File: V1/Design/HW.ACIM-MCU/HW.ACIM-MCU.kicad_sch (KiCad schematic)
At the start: 48 parts, among them J1 HEADER 2x15POS, J2 HEADER 2x15POS, U1 MIPS 32-bit DSC, U2 12MHz

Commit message: MCU PIM schematic update 5
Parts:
- removed C1, C11, C14, C15, C16, C17, C18, C2, C3, C4, C5, C6, C7, C8, C9: 22pF, SAMPI:CAP0402, symbol SAMPI:CERCAP
- removed R10, R11, R12, R13, R14, R2, R3, R4, R5, R6, R7, R8, R9: 10R, SAMPI:RES0402, symbol SAMPI:RES
- removed SH1, SH2: SCREW HOLDER, Liem:HOLDER-2.2MM, symbol SAMPI:SCREWHOLDER
- added D?: SLED, symbol SAMPI:RLED
- J1, J2: footprint SAMPI:HD-2x15x0.4-SMD -> SAMPI:HD-2x15x1.27-TH
- R1: value 10R -> 1K; footprint SAMPI:RES0402 -> (none)
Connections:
- net MC_IV_SENSE is gone; now on net MC_IV_SEN: J2.27
- net MC_IW is gone; now on net MC_VU_DIV: U1.16 (PGC3/OA1OUT/VREF+/AN3/C1IN4-/C4IN2-/RPB1/CTED1/RB1)
- net MC_IW_SENSE is gone; now on net MC_IW_SEN: J2.29
- net MC_VDC_SENSE is gone; now on net MC_VDC_DIV: J1.25
- net MC_VR_SENSE is gone; now on net MC_VR_DIV: J2.22
- net MC_VU_SENSE is gone; now on net MC_VU_DIV: J2.30
- net MC_VV_SENSE is gone; now on net MC_VV_DIV: J2.28
- net MC_VW_SENSE is gone; now on net MC_VW_DIV: J2.26
- net PFC_IB is gone; now on net MC_IU_SEN: U1.13 (OA2OUT/AN0/C2IN4-/C4IN3-/RPA0/RA0)
- net VAC_SENSE is gone; now on net VAC_DIV: J1.23
- net VREF_SENSE is gone; now on net VREF_DIV: J2.23
- net GND: now also D?.K
- net MC_VDC_DIV: no longer U1.45 (DAC2/AN48/CVD48/RPC10/PMA14/PMCS/RC10)
- net MC_VR_DIV: no longer U1.33 (OA5IN+/DAC1/AN24/CVD24/C5IN1+/C5IN3-/RPA4/RA4)
- net MC_VU_DIV: no longer U1.22 (OA3IN-/AN7/CVD7/C3IN1-/C4IN1-/RPC1/PMA7/RC1)
- net MC_VV_DIV: now also U1.17 (PGC1/OA1IN+/AN4/C1IN1+/C1IN3-/C2IN3-/RPB2/RB2); no longer U1.21 (OA3OUT/AN6/CVD6/C3IN4-/C4IN1+/C4IN4-/RPC0/RC0)
- net MC_VW_DIV: now also U1.18 (PGD1/OA1IN-/AN5/CTCMP/C1IN1-/RTCC/RPB3/RB3); no longer U1.23 (OA3IN+/AN8/CVD8/C3IN1+/C3IN3-/RPC2/FLT3/PMA13/RC2)
- net PFC_PWM_A: no longer U1.60 (RPB10/PWM3H/PMD0/RB10)
- net PFC_PWM_B: no longer U1.62 (RPB12/PWM2H/PMD2/RB12)
- net PFC_PWM_ENA: no longer U1.61 (RPB11/PWM9H/PWM3L/PMD1/RB11)
- net PFC_PWM_ENB: no longer U1.63 (RPB13/PWM8H/PWM2L/CTPLS/PMD3/RB13)
- net PGC: now also U1.43 (PGD2/RPB5/SDA3/USBID1/RB5); no longer U1.17 (PGC1/OA1IN+/AN4/C1IN1+/C1IN3-/C2IN3-/RPB2/RB2)
- net PGD: now also U1.44 (PGC2/RPB6/SCL3/SCK2/PMA15/RB6); no longer U1.18 (PGD1/OA1IN-/AN5/CTCMP/C1IN1-/RTCC/RPB3/RB3)
- net RXD1: no longer U1.44 (PGC2/RPB6/SCL3/SCK2/PMA15/RB6)
- net RXD2: no longer U1.43 (PGD2/RPB5/SDA3/USBID1/RB5)
- net SCK: now also J1.16; no longer J1.14
- net SDI: now also J1.14; no longer J1.12
- net SDO: now also J1.15; no longer J1.11
- net VAC_DIV: no longer U1.46 (OA5OUT/AN25/CVD25/C5IN4-/RPB7/SCK1/INT0/RB7)
- net VREF_DIV: no longer U1.24 (AN11/CVD11/C1IN2-/FLT4/PMA12/RC11)
- net IO3: now reaches J1.10
- net IO2: now reaches J1.9
- net GPIO1: no longer names the net of U1.2 (RPB14/PWM1H/VBUSON1/PMD6/RB14)
- net GPIO1: no longer J1.16
- net GPIO2: no longer names the net of U1.3 (RPB15/PWM7H/PWM1L/PMD7/RB15)
- net GPIO2: no longer J1.15
- net MC_IDC: no longer names the net of U1.49 (TMS/OA5IN-/AN27/CVD27/LVDIN/C5IN1-/RPB9/RB9)
- net MC_IDC_SENSE renamed MC_IDC_SEN
- net MC_IU renamed MC_IV_SEN
- net MC_IU_SENSE renamed MC_IU_SEN
- net MC_IV renamed MC_IW_SEN
- net MC_TEMP: no longer names the net of U1.11 (AN10/CVD10/RPA12/RA12)
- net MC_TEMP: no longer R1.2
- net MC_TEMP_SENSE: no longer names the net of R1.1
- net MC_TEMP_SENSE: now also D?.A; no longer J2.24
- net PFC_IA: no longer names the net of U1.12 (AN9/CVD9/RPA11/RA11)
- net PFC_IA_SENSE renamed PFC_IA_SEN
- net PFC_IA_SEN: now also U1.21 (OA3OUT/AN6/CVD6/C3IN4-/C4IN1+/C4IN4-/RPC0/RC0)
- net PFC_IB_SENSE renamed PFC_IB_SEN
- net PFC_IB_SEN: now also U1.22 (OA3IN-/AN7/CVD7/C3IN1-/C4IN1-/RPC1/PMA7/RC1)
- net ~{INV_FAULT}: no longer names the net of U1.58 (RPF0/PWM11H/RF0)
- net ~{INV_FLT_OC}: no longer names the net of U1.59 (RPF1/PWM11L/RF1)
- net ~{MEM_CFG} renamed ~{CS}
- new net IO0: J1.11
- new net IO1: J1.12
- new net MC_TEMP_SEN: J2.24
- new net PFC_IDC: U1.33 (OA5IN+/DAC1/AN24/CVD24/C5IN1+/C5IN3-/RPA4/RA4)
- new net SLED: R1.2
- no-connect marks 2 -> 0

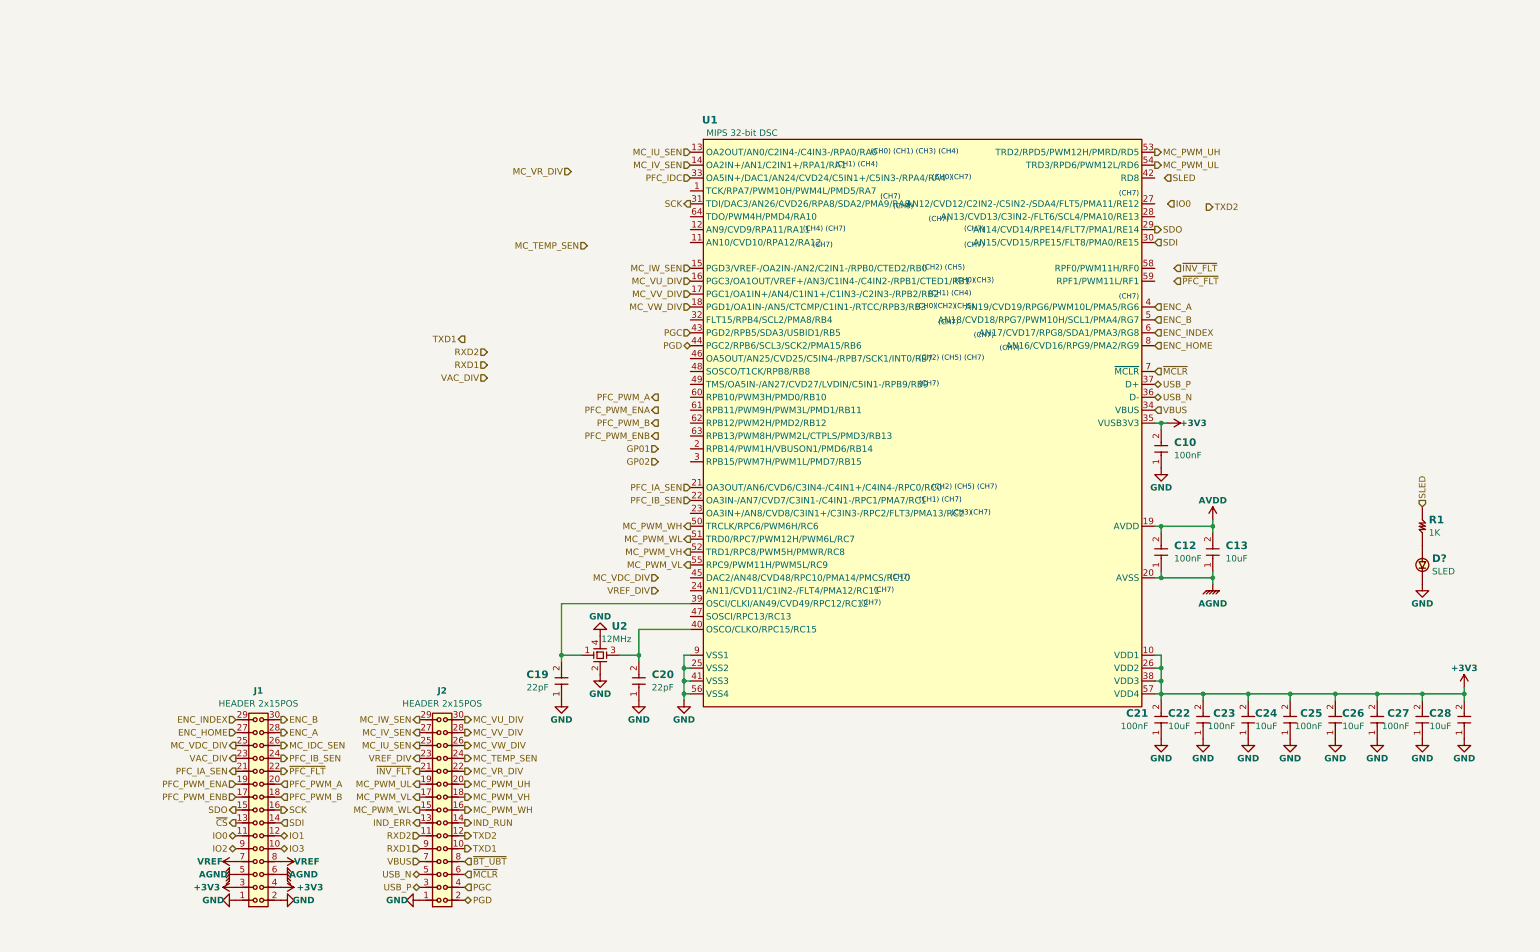
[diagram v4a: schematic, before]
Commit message: MCU PIM schematic update 6
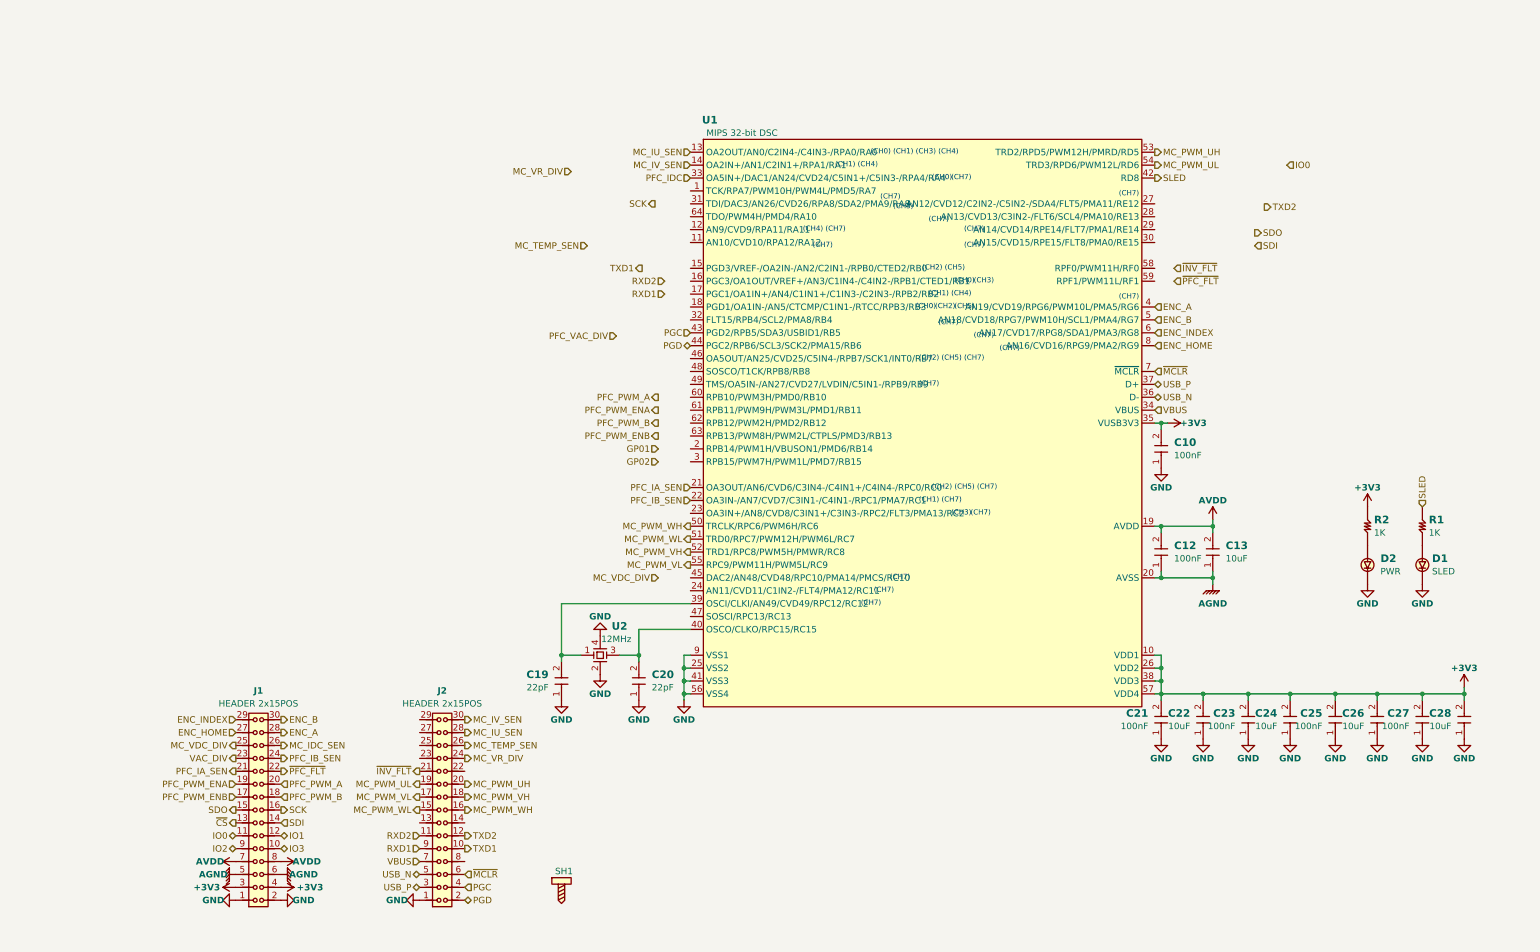
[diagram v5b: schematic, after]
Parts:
- added D2: PWR, SAMPI:LED0603, symbol SAMPI:RLED
- added R2: 1K, SAMPI:RES0402, symbol SAMPI:RES
- added SH1: SCREW HOLDER, SAMPI:HOLDER-2.2MM, symbol SAMPI:SCREWHOLDER
- D1: renamed from D?; footprint (none) -> SAMPI:LED0603
- R1: footprint (none) -> SAMPI:RES0402
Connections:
- net VREF is gone; now on net AVDD: J1.7, J1.8
- net +3V3: now also R2.2
- net GND: now also D2.K
- net MC_IU_SEN: now also J2.28; no longer J2.25
- net MC_IV_SEN: now also J2.30; no longer J2.27
- net MC_TEMP_SEN: now also J2.26; no longer J2.24
- net MC_VR_DIV: now also J2.24; no longer J2.22
- net SCK: no longer U1.31 (TDI/DAC3/AN26/CVD26/RPA8/SDA2/PMA9/RA8)
- net SDI: no longer U1.30 (AN15/CVD15/RPE15/FLT8/PMA0/RE15)
- net SDO: no longer U1.29 (AN14/CVD14/RPE14/FLT7/PMA1/RE14)
- net SLED: now also U1.42 (RD8)
- net IND_ERR: no longer names the net of J2.13
- net IND_RUN: no longer names the net of J2.14
- net MC_IW_SEN: no longer names the net of J2.29
- net MC_IW_SEN: no longer U1.15 (PGD3/VREF-/OA2IN-/AN2/C2IN1-/RPB0/CTED2/RB0)
- net MC_VU_DIV: no longer names the net of U1.16 (PGC3/OA1OUT/VREF+/AN3/C1IN4-/C4IN2-/RPB1/CTED1/RB1)
- net MC_VU_DIV: no longer J2.30
- net MC_VV_DIV: no longer names the net of U1.17 (PGC1/OA1IN+/AN4/C1IN1+/C1IN3-/C2IN3-/RPB2/RB2)
- net MC_VV_DIV: no longer J2.28
- net MC_VW_DIV: no longer names the net of U1.18 (PGD1/OA1IN-/AN5/CTCMP/C1IN1-/RTCC/RPB3/RB3)
- net MC_VW_DIV: no longer J2.26
- net VREF_DIV: no longer names the net of J2.23
- net ~{BT_UBT}: no longer names the net of J2.8
- new net: D2.A, R2.1

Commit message: MCU PIM schematic update 7
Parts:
- removed SH1: SCREW HOLDER, SAMPI:HOLDER-2.2MM, symbol SAMPI:SCREWHOLDER
- added C1: 22pF, SAMPI:CAP0402, symbol SAMPI:CERCAP
- added R3: 10K, SAMPI:RES0402, symbol SAMPI:RES
- D1: symbol SAMPI:RLED -> SAMPI:GLED
- J1, J2: footprint SAMPI:HD-2x15x1.27-TH -> SAMPI:HD-2x15x1.27-SMD
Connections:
- net MC_IDC_SEN is gone; now on net PFC_IA_SEN: J1.26
- net PFC_IDC is gone; now on net MC_IU_SEN: U1.33 (OA5IN+/DAC1/AN24/CVD24/C5IN1+/C5IN3-/RPA4/RA4)
- net +3V3: now also J2.27, J2.28, R3.2; no longer J1.3, J1.4
- net AGND: now also J1.1, J1.2; no longer J1.5, J1.6
- net AVDD: now also J1.3, J1.4; no longer J1.7, J1.8
- net GND: now also J2.29, J2.30, C1.1; no longer J1.1, J1.2, J2.1
- net IO0: no longer J1.11
- net MC_IU_SEN: now also J2.24; no longer J2.28, U1.13 (OA2OUT/AN0/C2IN4-/C4IN3-/RPA0/RA0)
- net MC_IV_SEN: now also J2.26, U1.31 (TDI/DAC3/AN26/CVD26/RPA8/SDA2/PMA9/RA8); no longer J2.30, U1.14 (OA2IN+/AN1/C2IN1+/RPA1/RA1)
- net MC_PWM_UH: now also J2.21; no longer J2.20
- net MC_PWM_UL: now also J2.22; no longer J2.19
- net MC_PWM_VH: now also J2.19; no longer J2.18
- net MC_PWM_VL: now also J2.20; no longer J2.17
- net MC_PWM_WH: now also J2.17; no longer J2.16
- net MC_PWM_WL: now also J2.18; no longer J2.15
- net MC_TEMP_SEN: now also J2.25, U1.49 (TMS/OA5IN-/AN27/CVD27/LVDIN/C5IN1-/RPB9/RB9); no longer J2.26
- net MC_VR_DIV: now also J2.23, U1.30 (AN15/CVD15/RPE15/FLT8/PMA0/RE15); no longer J2.24
- net PFC_IA_SEN: no longer J1.21
- net PGC: now also U1.44 (PGC2/RPB6/SCL3/SCK2/PMA15/RB6); no longer U1.43 (PGD2/RPB5/SDA3/USBID1/RB5)
- net PGD: now also U1.43 (PGD2/RPB5/SDA3/USBID1/RB5); no longer U1.44 (PGC2/RPB6/SCL3/SCK2/PMA15/RB6)
- net RXD1: now also J2.7, U1.47 (SOSCI/RPC13/RC13); no longer J2.9
- net RXD2: now also J2.9, U1.48 (SOSCO/T1CK/RPB8/RB8); no longer J2.11
- net TXD1: now also J2.8, U1.46 (OA5OUT/AN25/CVD25/C5IN4-/RPB7/SCK1/INT0/RB7); no longer J2.10
- net TXD2: now also J2.10, U1.45 (DAC2/AN48/CVD48/RPC10/PMA14/PMCS/RC10); no longer J2.12
- net USB_N: now also J2.3; no longer J2.5
- net USB_P: now also J2.5; no longer J2.3
- net VAC_DIV: now also J1.21; no longer J1.23
- net VBUS: now also J2.1; no longer J2.7
- net ~{INV_FLT}: now also J2.15, U1.59 (RPF1/PWM11L/RF1); no longer J2.21
- net ~{MCLR}: now also C1.2, R3.1
- net ENC_INDEX renamed ENC_IDX
- net IO1: no longer names the net of J1.12
- net IO2: no longer names the net of J1.9
- net IO3: no longer names the net of J1.10
- net MC_VDC_DIV renamed IDC_SEN
- net SCK: no longer names the net of J1.16
- net SDI: no longer names the net of J1.14
- net SDO: no longer names the net of J1.15
- net ~{CS}: no longer names the net of J1.13
- new net VDC_DIV: J1.23

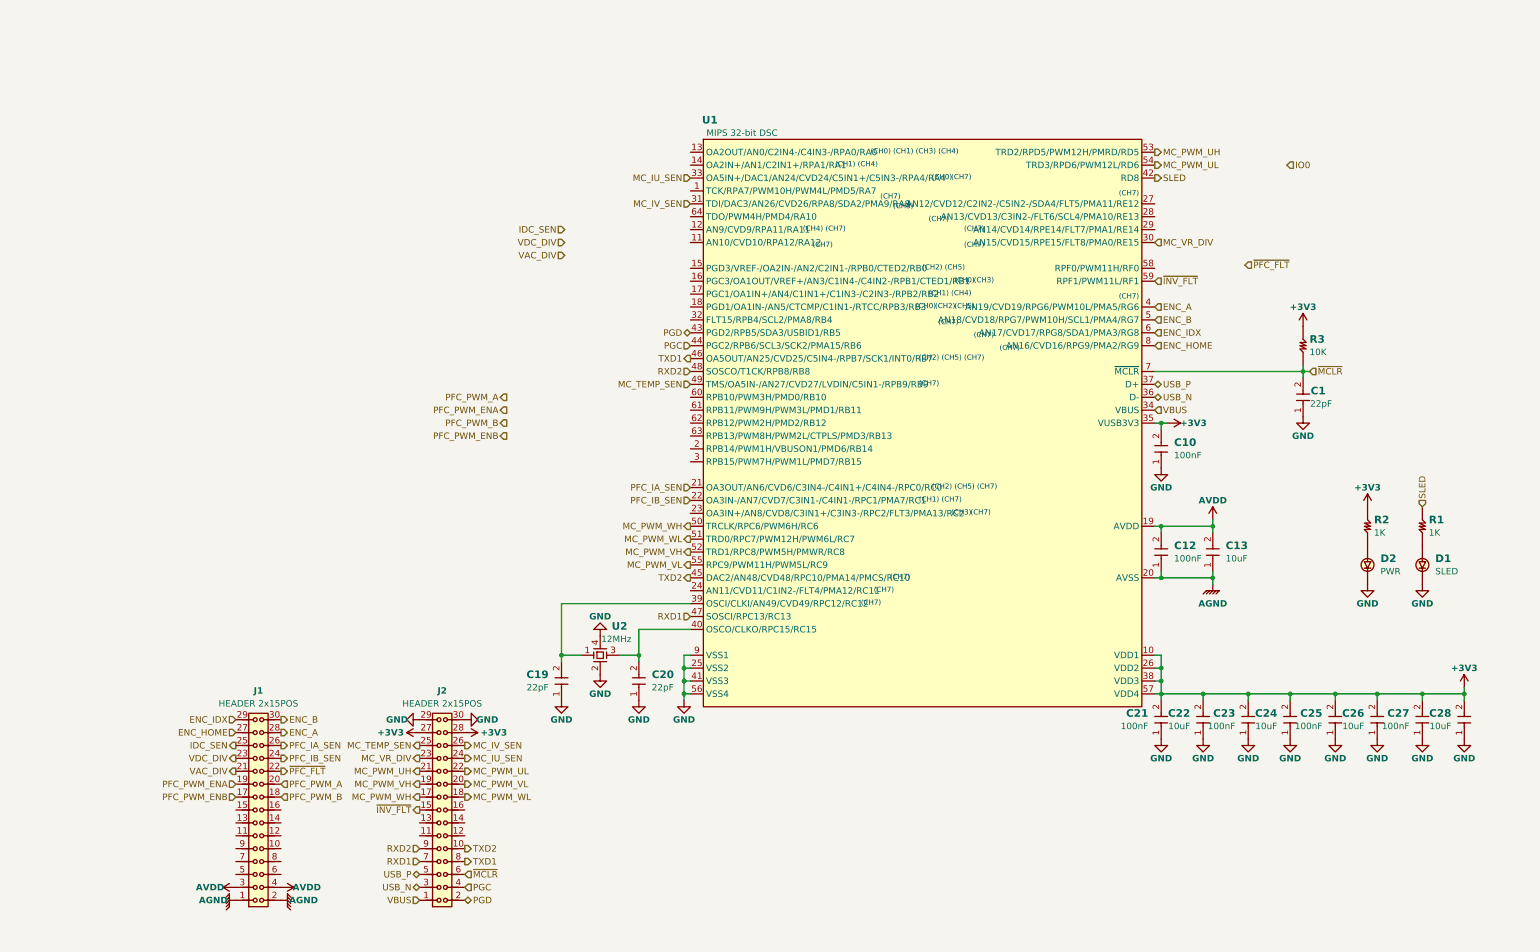
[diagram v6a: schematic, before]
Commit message: MCU PIM schematic update 8
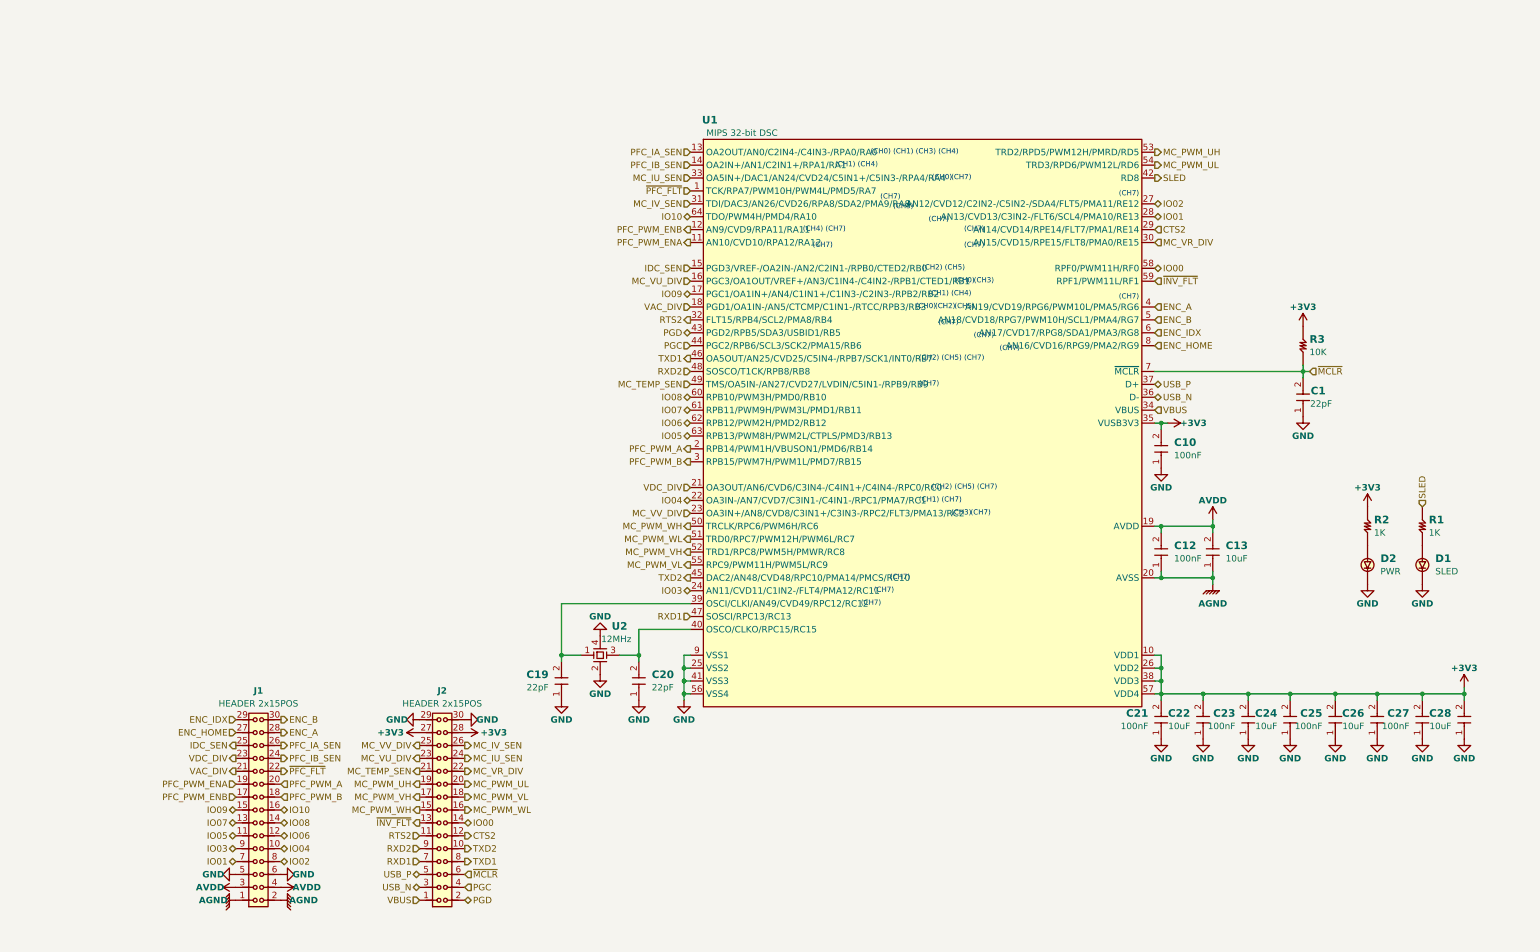
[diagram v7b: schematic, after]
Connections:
- net GND: now also J1.5, J1.6
- net IDC_SEN: now also U1.15 (PGD3/VREF-/OA2IN-/AN2/C2IN1-/RPB0/CTED2/RB0)
- net MC_PWM_UH: now also J2.19; no longer J2.21
- net MC_PWM_UL: now also J2.20; no longer J2.22
- net MC_PWM_VH: now also J2.17; no longer J2.19
- net MC_PWM_VL: now also J2.18; no longer J2.20
- net MC_PWM_WH: now also J2.15; no longer J2.17
- net MC_PWM_WL: now also J2.16; no longer J2.18
- net MC_TEMP_SEN: now also J2.21; no longer J2.25
- net MC_VR_DIV: now also J2.22; no longer J2.23
- net PFC_IA_SEN: now also U1.13 (OA2OUT/AN0/C2IN4-/C4IN3-/RPA0/RA0); no longer U1.21 (OA3OUT/AN6/CVD6/C3IN4-/C4IN1+/C4IN4-/RPC0/RC0)
- net PFC_IB_SEN: now also U1.14 (OA2IN+/AN1/C2IN1+/RPA1/RA1); no longer U1.22 (OA3IN-/AN7/CVD7/C3IN1-/C4IN1-/RPC1/PMA7/RC1)
- net PFC_PWM_A: now also U1.2 (RPB14/PWM1H/VBUSON1/PMD6/RB14)
- net PFC_PWM_B: now also U1.3 (RPB15/PWM7H/PWM1L/PMD7/RB15)
- net PFC_PWM_ENA: now also U1.11 (AN10/CVD10/RPA12/RA12)
- net PFC_PWM_ENB: now also U1.12 (AN9/CVD9/RPA11/RA11)
- net VAC_DIV: now also U1.18 (PGD1/OA1IN-/AN5/CTCMP/C1IN1-/RTCC/RPB3/RB3)
- net VDC_DIV: now also U1.21 (OA3OUT/AN6/CVD6/C3IN4-/C4IN1+/C4IN4-/RPC0/RC0)
- net ~{INV_FLT}: now also J2.13; no longer J2.15
- net ~{PFC_FLT}: now also U1.1 (TCK/RPA7/PWM10H/PWM4L/PMD5/RA7)
- net RTS2: now reaches J2.11
- net RTS2: now also U1.32 (FLT15/RPB4/SCL2/PMA8/RB4)
- net CTS2: now reaches J2.12
- net CTS2: now also U1.29 (AN14/CVD14/RPE14/FLT7/PMA1/RE14)
- net IO00: now reaches J2.14
- net IO00: now also U1.58 (RPF0/PWM11H/RF0)
- net IO04: now reaches J1.10
- net IO04: now also U1.22 (OA3IN-/AN7/CVD7/C3IN1-/C4IN1-/RPC1/PMA7/RC1)
- net IO05: now reaches J1.11
- net IO05: now also U1.63 (RPB13/PWM8H/PWM2L/CTPLS/PMD3/RB13)
- net IO06: now reaches J1.12
- net IO06: now also U1.62 (RPB12/PWM2H/PMD2/RB12)
- net IO07: now reaches J1.13
- net IO07: now also U1.61 (RPB11/PWM9H/PWM3L/PMD1/RB11)
- net IO08: now reaches J1.14
- net IO08: now also U1.60 (RPB10/PWM3H/PMD0/RB10)
- net IO09: now reaches J1.15
- net IO09: now also U1.17 (PGC1/OA1IN+/AN4/C1IN1+/C1IN3-/C2IN3-/RPB2/RB2)
- net IO10: now reaches J1.16
- net IO10: now also U1.64 (TDO/PWM4H/PMD4/RA10)
- net IO01: now reaches J1.7
- net IO01: now also U1.28 (AN13/CVD13/C3IN2-/FLT6/SCL4/PMA10/RE13)
- net IO02: now reaches J1.8
- net IO02: now also U1.27 (AN12/CVD12/C2IN2-/C5IN2-/SDA4/FLT5/PMA11/RE12)
- net IO03: now reaches J1.9
- net IO03: now also U1.24 (AN11/CVD11/C1IN2-/FLT4/PMA12/RC11)
- net MC_VU_DIV: now reaches U1.16 (PGC3/OA1OUT/VREF+/AN3/C1IN4-/C4IN2-/RPB1/CTED1/RB1)
- net MC_VU_DIV: now also J2.23
- net MC_VV_DIV: now reaches U1.23 (OA3IN+/AN8/CVD8/C3IN1+/C3IN3-/RPC2/FLT3/PMA13/RC2)
- net MC_VV_DIV: now also J2.25
